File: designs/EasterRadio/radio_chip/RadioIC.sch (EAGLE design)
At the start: 40 parts, among them J1 S2B-NSHSS-TB, J2 S2B-NSHSS-TB, J3 S2B-NSHSS-TB, Q1 2SC3838T146, Y1 32.768kHz crystal

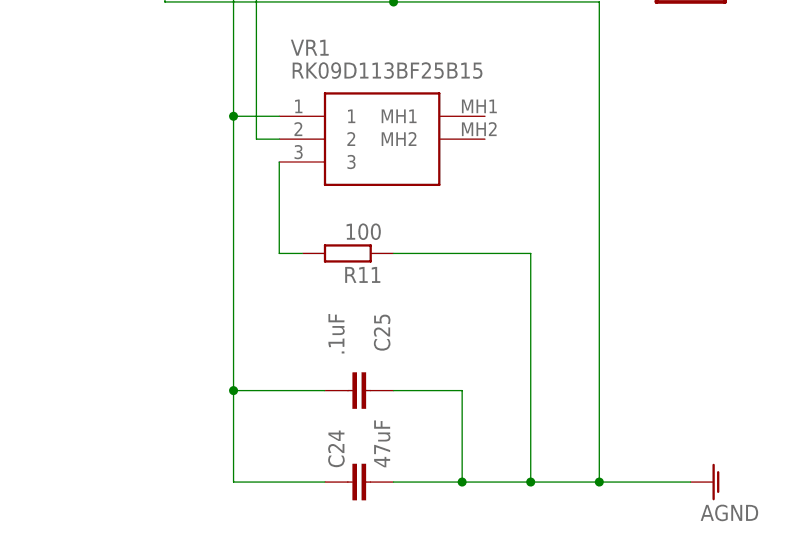
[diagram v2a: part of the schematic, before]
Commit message: Added comments to radioIC.sch
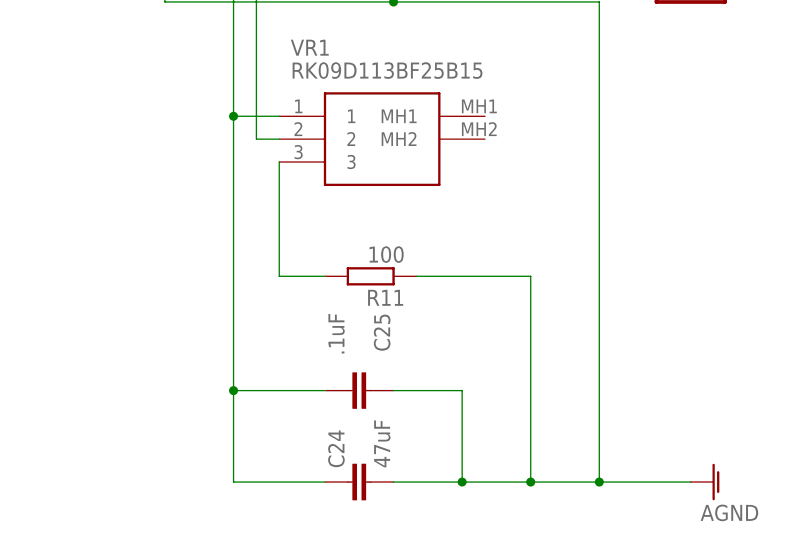
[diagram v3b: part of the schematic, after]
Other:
- note added: "Connection to Audio Speaker"
- note added: "IRQ to uC: active high"
- note added: "I²C to uC"
- note added: "Jumpers only necessary due to space issues. Should be removed."
- note added: "Potentiometer to adjust receiver frequency"
- moved on the sheet: R11
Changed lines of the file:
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@@
 <?xml version="1.0" encoding="utf-8"?>
 <!DOCTYPE eagle SYSTEM "eagle.dtd">
-<eagle version="9.6.1">
+<eagle version="9.6.2">
 <drawing>
 <settings>
@@
 <text x="170.18" y="152.4" size="2.54" layer="91">Power</text>
 <text x="0" y="210.82" size="5.08" layer="91">Radio IC (SI4840-A10-GU)</text>
+<text x="53.34" y="43.18" size="1.778" layer="89">Potentiometer
+to adjust receiver frequency</text>
+<text x="132.08" y="121.92" size="1.778" layer="89">Connection to
+Audio Speaker</text>
+<text x="187.96" y="190.5" size="1.778" layer="89">I²C to uC</text>
+<text x="187.96" y="175.26" size="1.778" layer="89">IRQ to uC:
+active high</text>
+<text x="114.3" y="139.7" size="1.778" layer="89">Jumpers only necessary
+due to space issues.
+Should be removed.</text>
+<text x="116.84" y="22.86" size="1.778" layer="89">Jumpers only necessary
+due to space issues.
+Should be removed.</text>
 </plain>
 <instances>
@@
 <attribute name="VALUE" x="52.07" y="60.96" size="1.778" layer="96" align="center-left"/>
 </instance>
-<instance part="R11" gate="G$1" x="58.42" y="40.64" smashed="yes" rot="R180">
-<attribute name="NAME" x="62.23" y="39.1414" size="1.778" layer="95" rot="R180"/>
-<attribute name="VALUE" x="62.23" y="43.942" size="1.778" layer="96" rot="R180"/>
+<instance part="R11" gate="G$1" x="60.96" y="38.1" smashed="yes" rot="R180">
+<attribute name="NAME" x="64.77" y="36.6014" size="1.778" layer="95" rot="R180"/>
+<attribute name="VALUE" x="64.77" y="41.402" size="1.778" layer="96" rot="R180"/>
 </instance>
 <instance part="C24" gate="G$1" x="58.42" y="15.24" smashed="yes" rot="R90">
@@
 <segment>
 <pinref part="R11" gate="G$1" pin="1"/>
-<wire x1="63.5" y1="40.64" x2="78.74" y2="40.64" width="0.1524" layer="91"/>
-<wire x1="78.74" y1="40.64" x2="78.74" y2="15.24" width="0.1524" layer="91"/>
+<wire x1="66.04" y1="38.1" x2="78.74" y2="38.1" width="0.1524" layer="91"/>
+<wire x1="78.74" y1="38.1" x2="78.74" y2="15.24" width="0.1524" layer="91"/>
 <pinref part="AGND10" gate="VR1" pin="AGND"/>
 <pinref part="C25" gate="G$1" pin="1"/>
@@
 <pinref part="VR1" gate="G$1" pin="3"/>
 <pinref part="R11" gate="G$1" pin="2"/>
-<wire x1="50.8" y1="50.8" x2="50.8" y2="40.64" width="0.1524" layer="91"/>
-<wire x1="50.8" y1="40.64" x2="53.34" y2="40.64" width="0.1524" layer="91"/>
+<wire x1="50.8" y1="50.8" x2="50.8" y2="38.1" width="0.1524" layer="91"/>
+<wire x1="50.8" y1="38.1" x2="55.88" y2="38.1" width="0.1524" layer="91"/>
 </segment>
 </net>
@@
 </drawing>
 <compatibility>
+<note version="6.3" minversion="6.2.2" severity="warning">
+Since Version 6.2.2 text objects can contain more than one line,
+which will not be processed correctly with this version.
+</note>
 <note version="8.2" severity="warning">
 Since Version 8.2, EAGLE supports online libraries. The ids

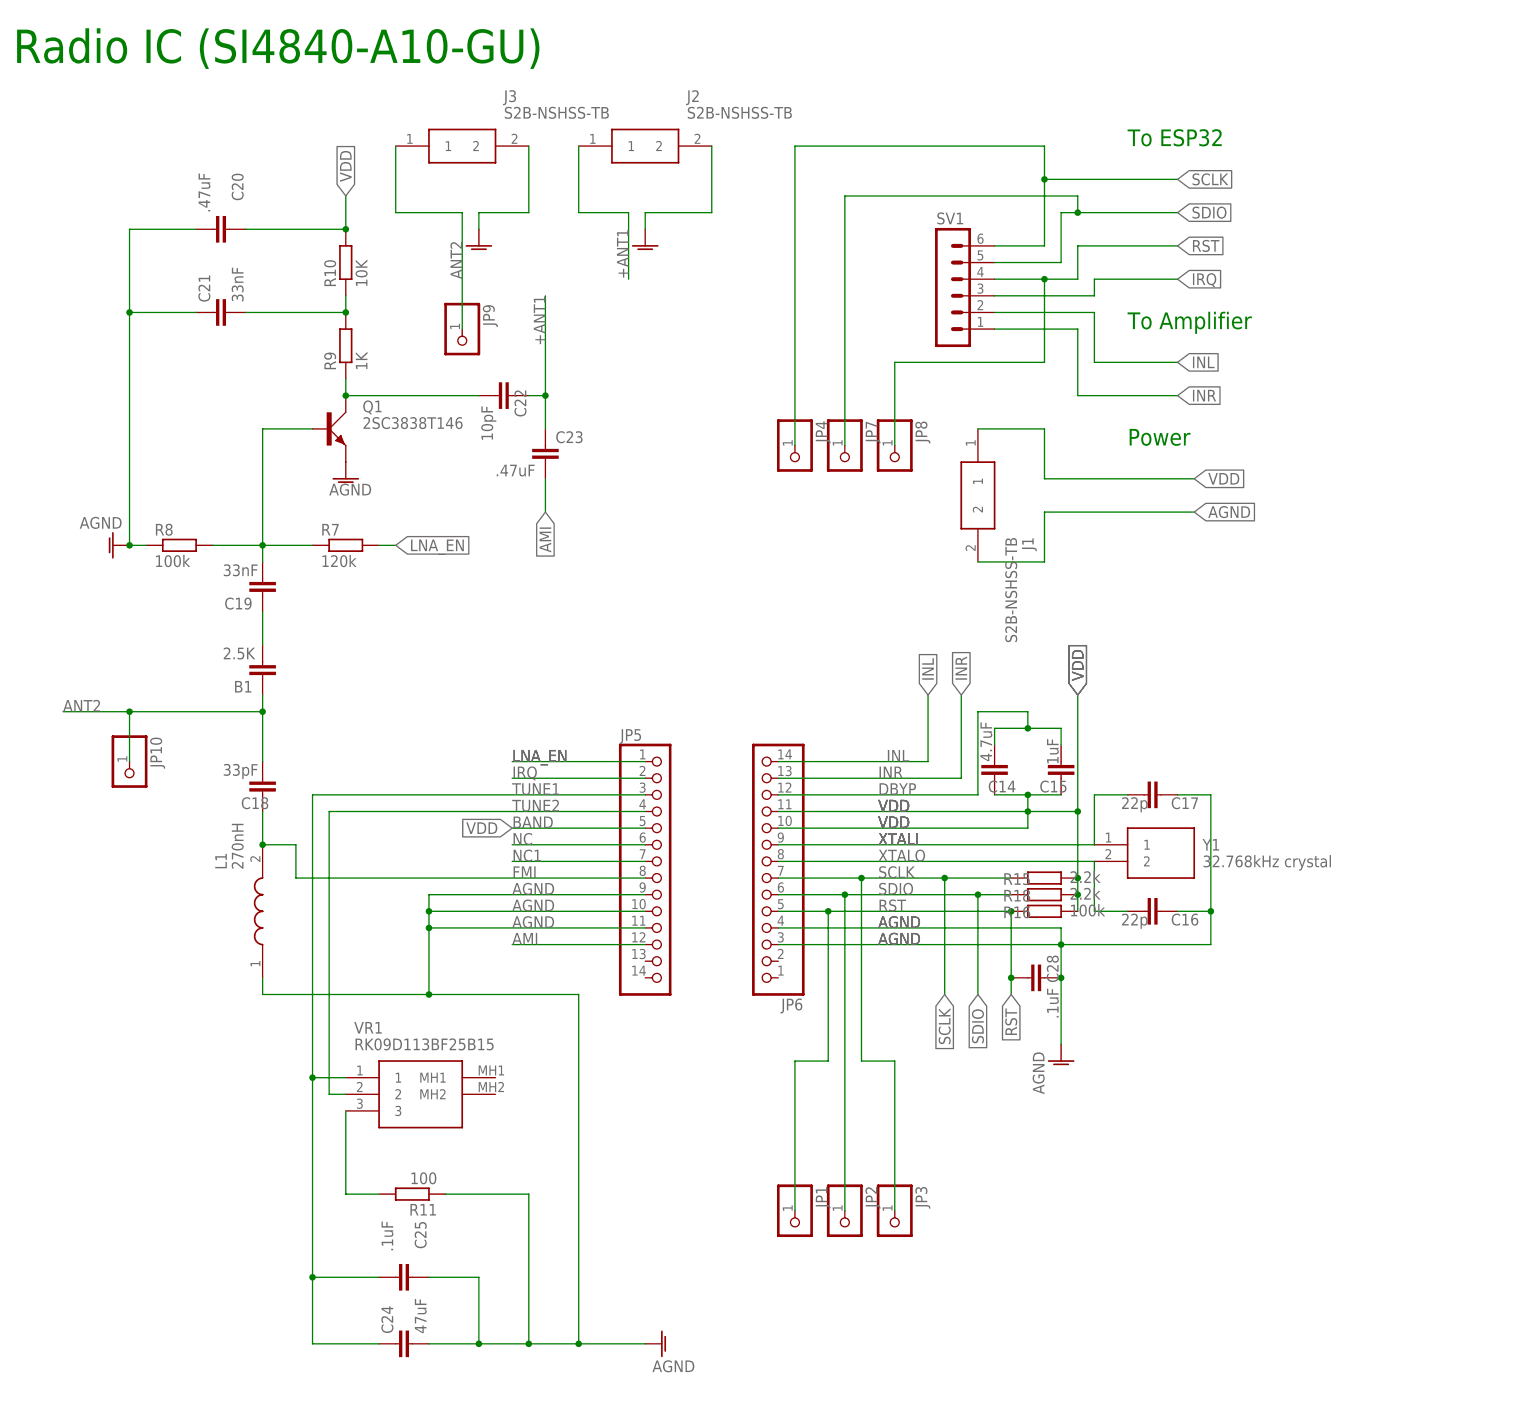
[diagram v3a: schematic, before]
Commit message: added Poti and Encoder pcb
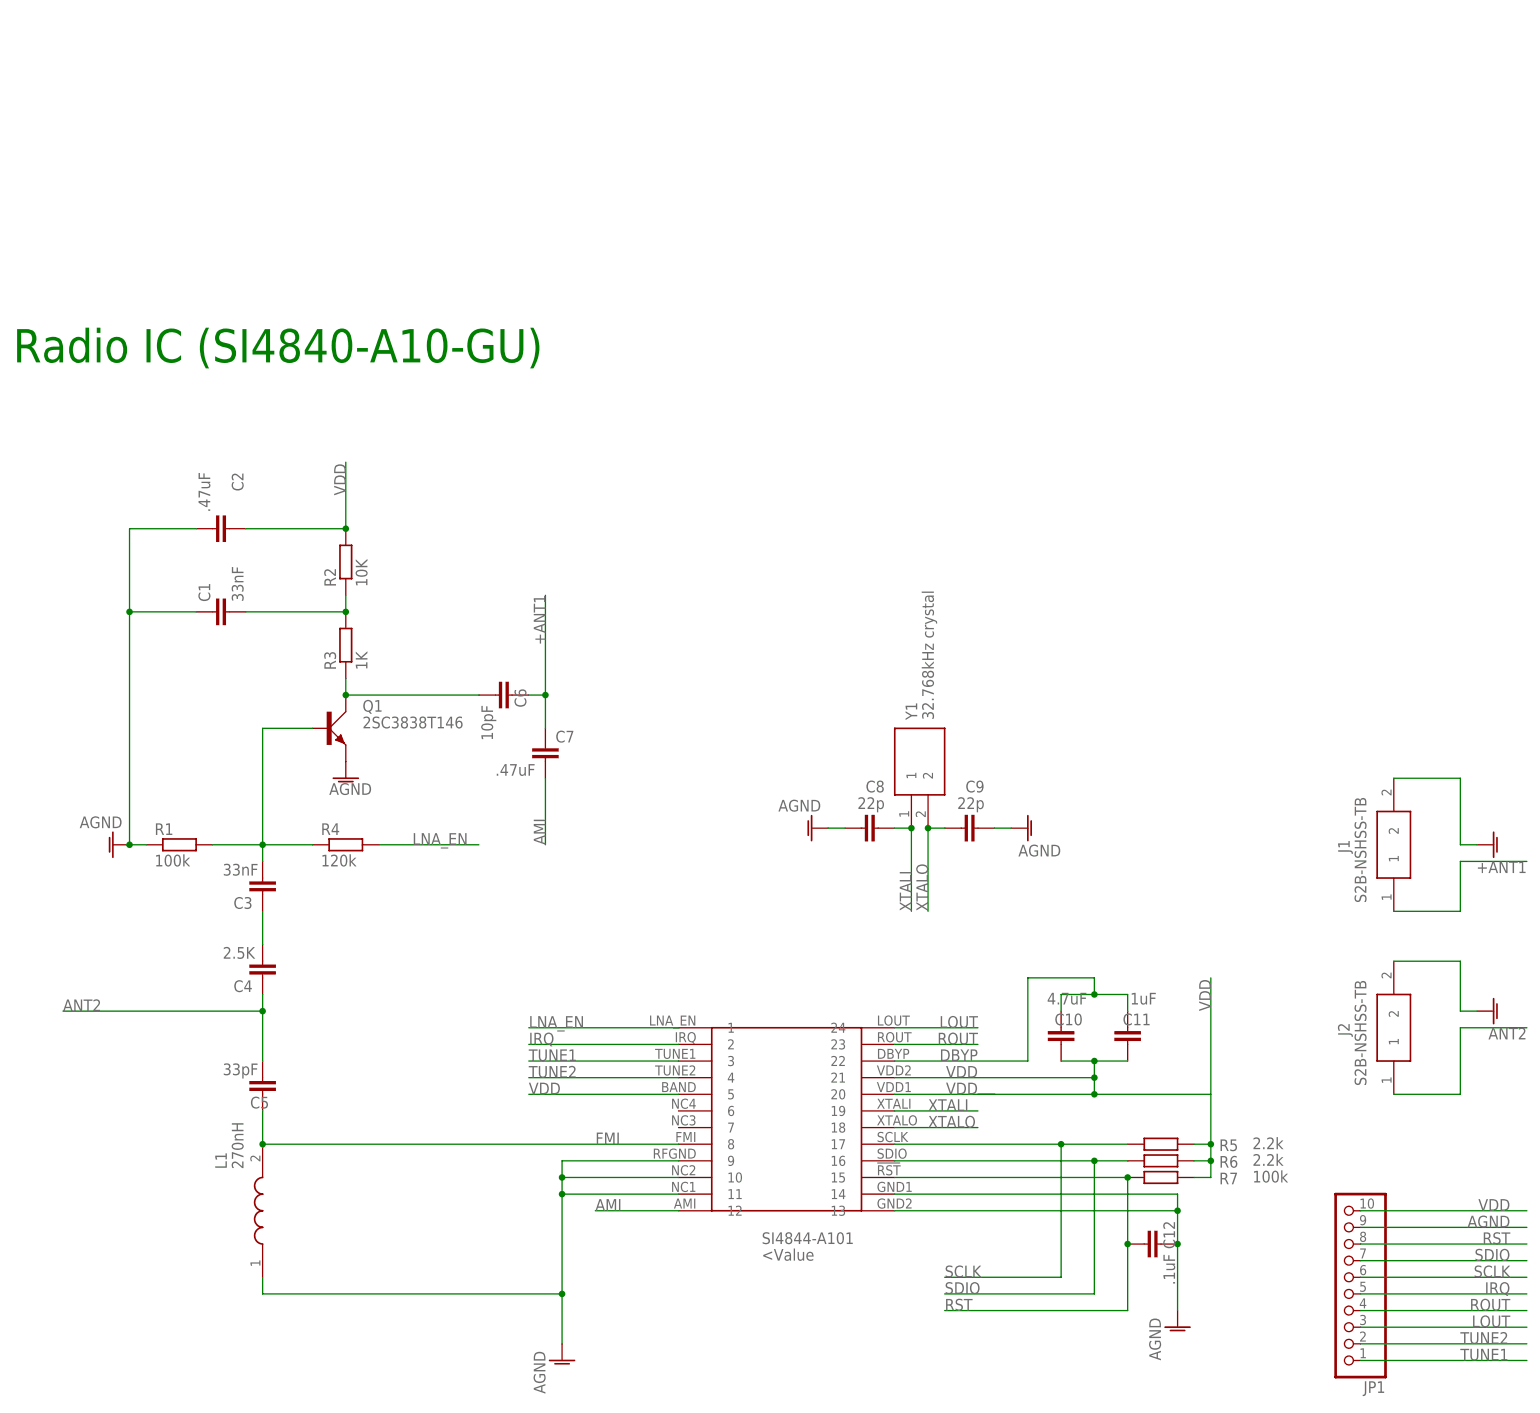
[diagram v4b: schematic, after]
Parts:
- removed B1: 2.5K, CommonParts:C-EU_805C0805
- removed C14: 4.7uF, CommonParts:C-EU_1206C1206
- removed C15: 1uF, CommonParts:C-EU_805C0805
- removed C16, C17: 22p, CommonParts:C-EU_805C0805
- removed C18: 33pF, CommonParts:C-EU_805C0805
- removed C19: 33nF, CommonParts:C-EU_1206C1206
- removed C20, C23: .47uF, CommonParts:C-EU_805C0805
- removed C21: 33nF, MouserUseful:CNC5L1X7R1C106K160AEC1206
- removed C22: 10pF, CommonParts:C-EU_805C0805
- removed C24: 47uF, MouserUseful:CNC5L1X7R1C106K160AEC1206
- removed C25, C28: .1uF, CommonParts:C-EU_805C0805
- removed J3: S2B-NSHSS-TB, CommonParts:S2B-NSHSS-TB
- removed JP10, JP2, JP3, JP4, JP7, JP8, JP9: (no value), pinhead:PINHD-1X1
- removed JP5, JP6: (no value), pinhead:PINHD-1X14
- removed R10: 10K, MouserUseful:RCS1206100KJNEAR1206
- removed R11: 100, MouserUseful:ERJ-PB6B5623VR0805
- removed R15, R18: 2.2k, MouserUseful:ERJ-PB6B5623VR0805
- removed R16, R8: 100k, MouserUseful:ERJ-PB6B5623VR0805
- removed R9: 1K, MouserUseful:RCS1206100KJNEAR1206
- removed SV1: (no value), con-lstb:MA06-1
- removed VR1: RK09D113BF25B15, MouserUseful:RK09D113BF25B15
- added C1: 33nF, MouserUseful:CNC5L1X7R1C106K160AEC1206
- added C10: 4.7uF, CommonParts:C-EU_1206C1206
- added C11: 1uF, CommonParts:C-EU_805C0805
- added C12: .1uF, CommonParts:C-EU_805C0805
- added C2, C7: .47uF, CommonParts:C-EU_805C0805
- added C3: 33nF, CommonParts:C-EU_1206C1206
- added C4: 2.5K, CommonParts:C-EU_805C0805
- added C5: 33pF, CommonParts:C-EU_805C0805
- added C6: 10pF, CommonParts:C-EU_805C0805
- added C8, C9: 22p, CommonParts:C-EU_805C0805
- added R1: 100k, MouserUseful:ERJ-PB6B5623VR0805
- added R2: 10K, MouserUseful:RCS1206100KJNEAR1206
- added R3: 1K, MouserUseful:RCS1206100KJNEAR1206
- added R4: 120k, MouserUseful:ERJ-PB6B5623VR0805
- added R5, R6: 2.2k, MouserUseful:ERJ-PB6B5623VR0805
- added SI4844-A101: (no value), MouserUseful:SI4840-A10-GU
- JP1: device pinhead:PINHD-1X1 -> pinhead:PINHD-1X10
- R7: value 120k -> 100k
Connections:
- removed net BAND: JP5.5
- removed net INL: JP6.14, SV1.2
- removed net INR: JP6.13, SV1.1
- removed net N$8: C20.1, R10.2
- removed net N$9: R11.2, VR1.3
- removed net NC: JP5.6
- removed net NC1: JP5.7
- new net LOUT: JP1.3, SI4844-A101.24
- new net ROUT: JP1.4, SI4844-A101.23
- net +ANT1: now also C6.1, C7.1, J1.1; no longer C22.1, C23.1, J2.1
- net AGND: now also C1.1, C12.1, C2.2, C8.1, C9.2, JP1.9, R1.1, SI4844-A101.10, SI4844-A101.11, SI4844-A101.13, SI4844-A101.14, SI4844-A101.9; no longer C16.1, C17.1, C20.2, C21.1, C24.2, C25.1, C28.1, J3.2, JP5.10, JP5.11, JP5.9, JP6.3, JP6.4, R11.1, R8.1
- net AMI: now also C7.2, SI4844-A101.12; no longer C23.2, JP5.12
- net ANT2: now also C4.1, C5.2, J2.1; no longer B1.1, C18.2, J3.1, JP10.1, JP9.1
- net DBYP: now also C10.2, C11.2, SI4844-A101.22; no longer C14.2, C15.2, JP6.12
- net FMI: now also C5.1, SI4844-A101.8; no longer C18.1, JP5.8
- net IRQ: now also JP1.5, SI4844-A101.2; no longer JP5.2, SV1.3
- net LNA_EN: now also R4.2, SI4844-A101.1; no longer JP5.1, R7.2
- net N$3: now also C3.1, C4.2; no longer B1.2, C19.1
- net N$5: now also C3.2, R1.2, R4.1; no longer C19.2, R7.1, R8.2
- net N$6: now also C6.2, R3.1; no longer C22.2, R9.1
- net N$7: now also C1.2, R2.1, R3.2; no longer C21.2, R10.1, R9.2
- net RST: now also C12.2, JP1.8, R7.1, SI4844-A101.15; no longer C28.2, JP1.1, JP6.5, JP8.1, R16.1, SV1.4
- net SCLK: now also JP1.6, R5.1, SI4844-A101.17; no longer JP3.1, JP4.1, JP6.7, R15.1, SV1.6
- net SDIO: now also JP1.7, R6.1, SI4844-A101.16; no longer JP2.1, JP6.6, JP7.1, R18.1, SV1.5
- net TUNE1: now also JP1.1, SI4844-A101.3; no longer C24.1, C25.2, JP5.3, VR1.1
- net TUNE2: now also JP1.2, SI4844-A101.4; no longer JP5.4, VR1.2
- net VDD: now also C10.1, C11.1, C2.1, JP1.10, R2.2, R5.2, R6.2, R7.2, SI4844-A101.20, SI4844-A101.21, SI4844-A101.5; no longer C14.1, C15.1, J1.1, JP6.10, JP6.11, R15.2, R16.2, R18.2
- net XTALI: now also C8.2, SI4844-A101.19; no longer C17.2, JP6.9
- net XTALO: now also C9.1, SI4844-A101.18; no longer C16.2, JP6.8
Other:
- note removed: "Connection to Audio Speaker"
- note removed: "IRQ to uC: active high"
- note removed: "I²C to uC"
- note removed: "Jumpers only necessary due to space issues. Should be removed."
- note removed: "Potentiometer to adjust receiver frequency"
- note removed: "Power"
- note removed: "To Amplifier"
- note removed: "To ESP32"
- moved on the sheet: J1, J2, L1, Q1, R7, Y1

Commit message: changes for new design excluding swap for amplifier
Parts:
- B1: value 2.5K -> 2.5K Ferrit Perle
- renumbered C4 to B1
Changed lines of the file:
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@@
 <part name="C5" library="CommonParts" deviceset="C-EU_805" device="C0805" package3d_urn="urn:adsk.eagle:package:23617/2" value="33pF"/>
 <part name="C3" library="CommonParts" deviceset="C-EU_1206" device="C1206" package3d_urn="urn:adsk.eagle:package:23618/2" value="33nF"/>
-<part name="C4" library="CommonParts" deviceset="C-EU_805" device="C0805" package3d_urn="urn:adsk.eagle:package:23617/2" value="2.5K"/>
+<part name="B1" library="CommonParts" deviceset="C-EU_805" device="C0805" package3d_urn="urn:adsk.eagle:package:23617/2" value="2.5K Ferrit Perle"/>
 <part name="AGND7" library="supply1" library_urn="urn:adsk.eagle:library:371" deviceset="AGND" device=""/>
 <part name="R4" library="MouserUseful" deviceset="ERJ-PB6B5623V" device="R0805" package3d_urn="urn:adsk.eagle:package:23553/2" value="120k"/>
@@
 <attribute name="VALUE" x="32.004" y="86.741" size="1.778" layer="96"/>
 </instance>
-<instance part="C4" gate="G$1" x="38.1" y="71.12" smashed="yes" rot="R180" grouprefs="SI4844">
+<instance part="B1" gate="G$1" x="38.1" y="71.12" smashed="yes" rot="R180" grouprefs="SI4844">
 <attribute name="NAME" x="36.576" y="70.739" size="1.778" layer="95" rot="R180"/>
 <attribute name="VALUE" x="32.004" y="74.041" size="1.778" layer="96"/>
@@
 <pinref part="C5" gate="G$1" pin="2"/>
 <wire x1="38.1" y1="58.42" x2="38.1" y2="66.04" width="0.1524" layer="91" grouprefs="SI4844"/>
-<pinref part="C4" gate="G$1" pin="1"/>
+<pinref part="B1" gate="G$1" pin="1"/>
 <wire x1="38.1" y1="68.58" x2="38.1" y2="66.04" width="0.1524" layer="91" grouprefs="SI4844"/>
 <junction x="38.1" y="66.04" grouprefs="SI4844"/>
@@
 <segment>
 <pinref part="C3" gate="G$1" pin="1"/>
-<pinref part="C4" gate="G$1" pin="2"/>
+<pinref part="B1" gate="G$1" pin="2"/>
 <wire x1="38.1" y1="81.28" x2="38.1" y2="76.2" width="0.1524" layer="91" grouprefs="SI4844"/>
 </segment>

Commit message: added final revisions to amplifier power radio ic and control pcbs
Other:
- note added: "Revision 1 02.04.21"
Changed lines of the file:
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@@
 <text x="0" y="165.1" size="5.08" layer="91">Radio IC (SI4840-A10-GU)</text>
 <frame x1="0" y1="0" x2="241.3" y2="162.56" columns="8" rows="5" layer="91"/>
+<text x="86.36" y="165.1" size="1.778" layer="91">Revision 1 02.04.21</text>
 </plain>
 <instances>
